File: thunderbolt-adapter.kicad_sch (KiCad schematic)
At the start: 16 parts

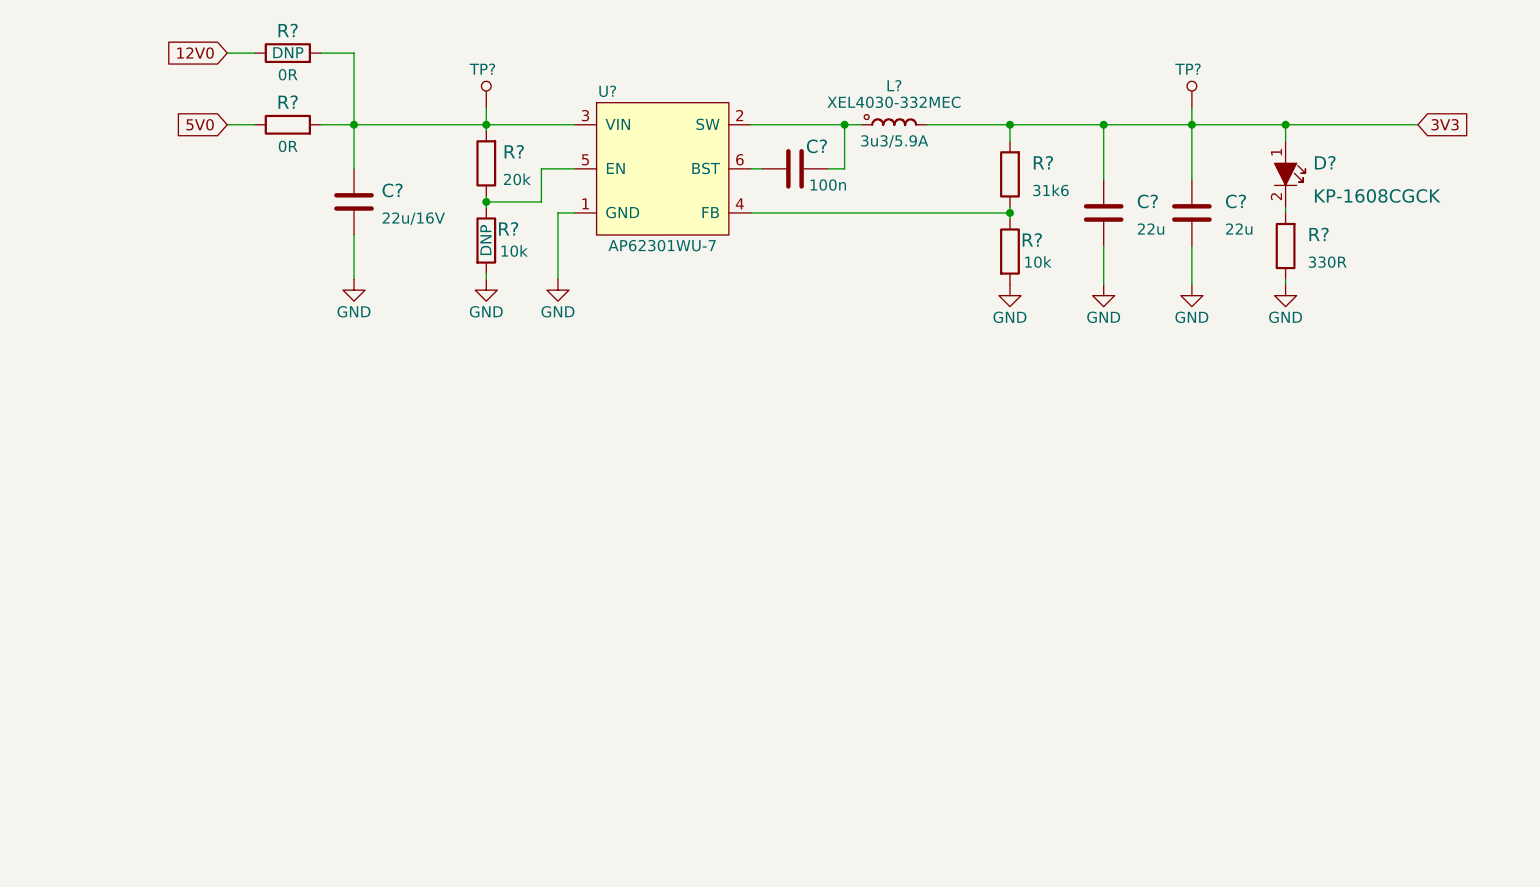
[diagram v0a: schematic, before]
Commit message: Add PCIe clock generator
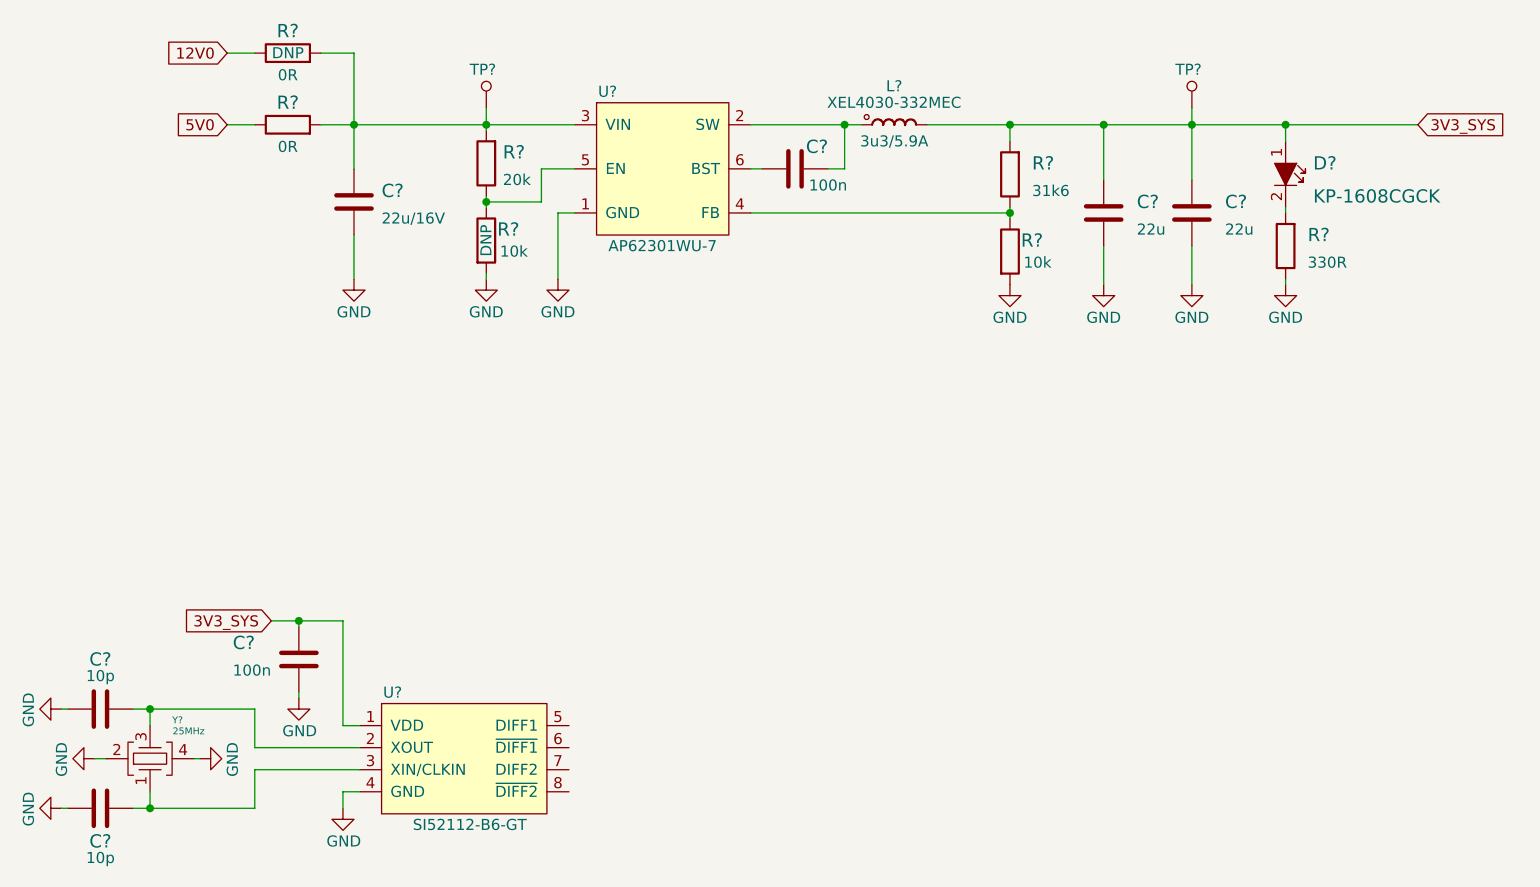
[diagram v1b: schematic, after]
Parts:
- added C? (x2): C_10p_0402, antmicro-footprints:0402-cap, symbol antmicroCapacitors0402:C_10p_0402
- added C?: C_100n_0402, antmicro-footprints:0402-cap, symbol antmicroCapacitors0402:C_100n_0402
- added U?: SI52112-B6-GT, antmicro-footprints:TSSOP-8_W4.4mm, symbol antmicroClockTimingClockGeneratorsPLLsFrequencySynthesizers:SI52112-B6-GT
- added Y?: 25MHz, antmicro-footprints:KX-7, symbol antmicroCrystals:ABM8G-25.000MHZ-B4Y-T
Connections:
- net GND: now also C?.1, C?.1, C?.2, U?.4 (GND), Y?.2, Y?.4
- net 3V3 renamed 3V3_SYS
- net 3V3_SYS: now also C?.1, U?.1 (VDD)
- new net: C?.2, U?.2 (XOUT), Y?.3
- new net: C?.2, U?.3 (XIN/CLKIN), Y?.1

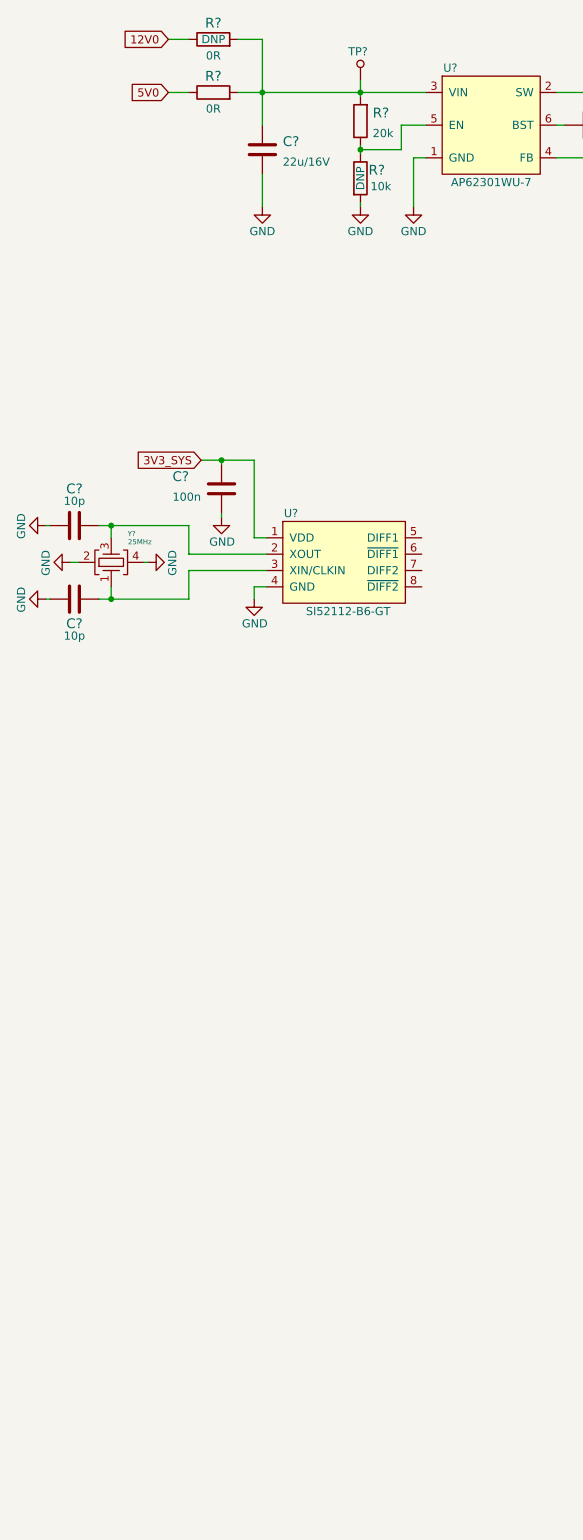
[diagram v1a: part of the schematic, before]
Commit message: Add USB-C connector
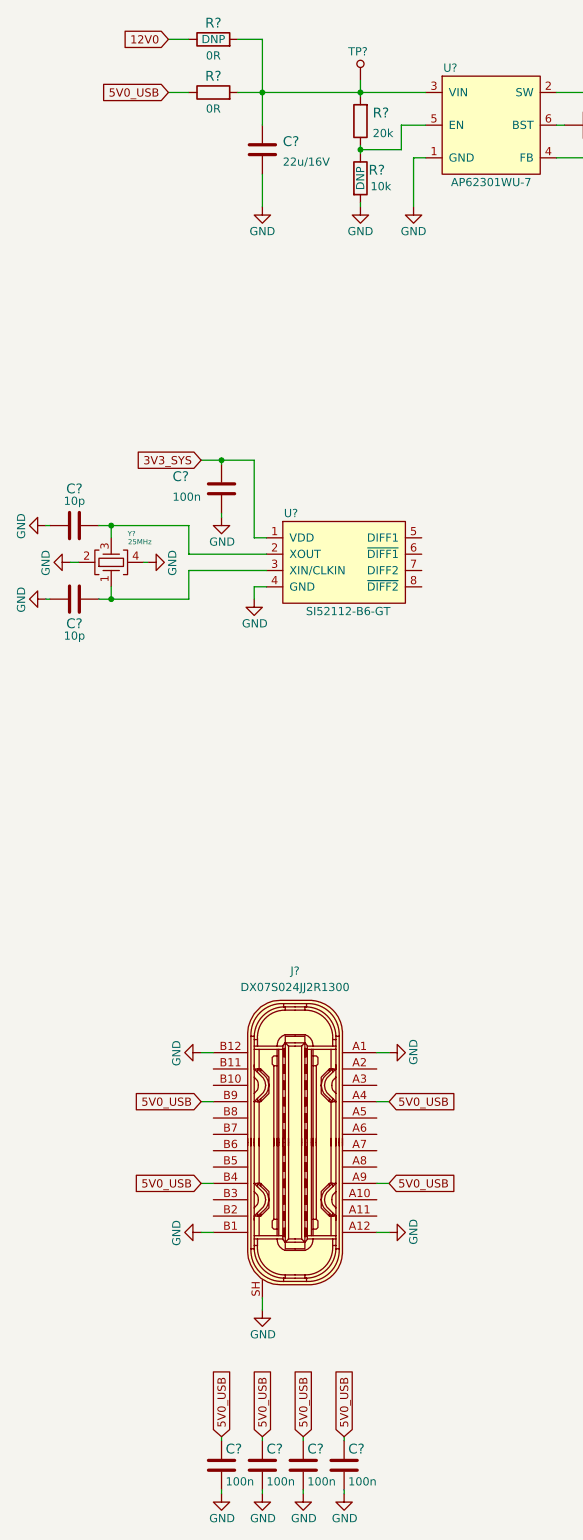
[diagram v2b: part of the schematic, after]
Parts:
- added C? (x4): C_100n_0402, antmicro-footprints:0402-cap, symbol antmicroCapacitors0402:C_100n_0402
- added J?: DX07S024JJ2R1300, antmicro-footprints:DX07S024JJ2R1300, symbol antmicroUSBDVIHDMIConnectors:DX07S024JJ2R1300
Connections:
- net GND: now also C?.2, C?.2, C?.2, C?.2, J?.A1, J?.A12, J?.B1, J?.B12, J?.SH
- net 5V0 renamed 5V0_USB
- net 5V0_USB: now also C?.1, C?.1, C?.1, C?.1, J?.A4, J?.A9, J?.B4, J?.B9

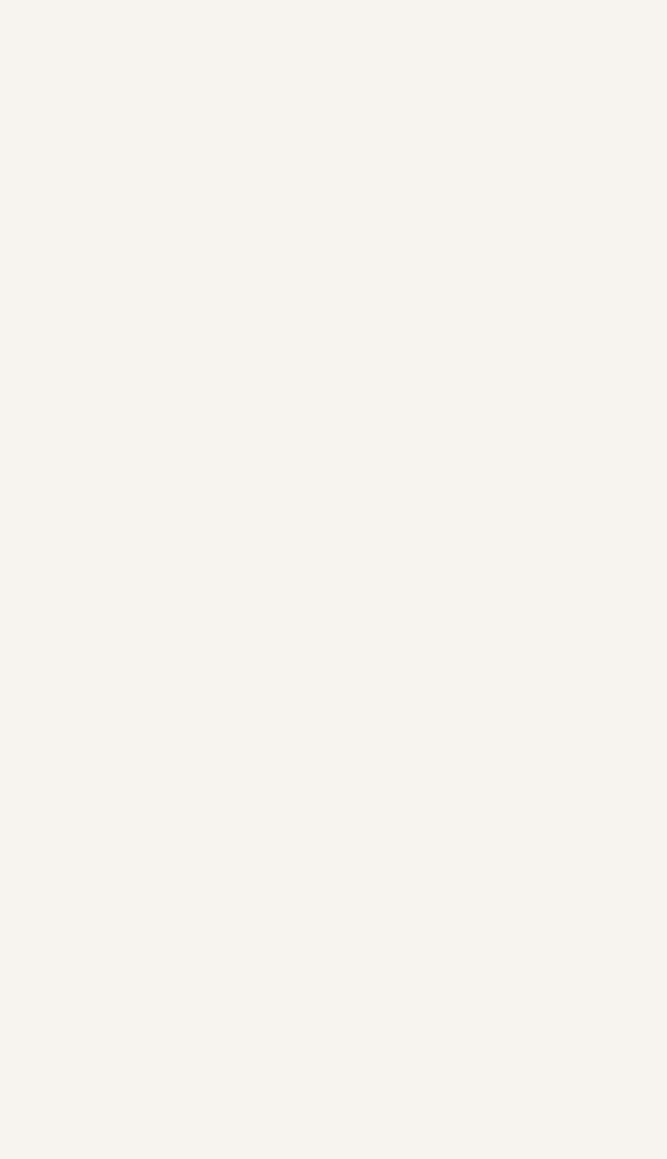
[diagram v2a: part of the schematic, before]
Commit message: Add PCIe edge connector
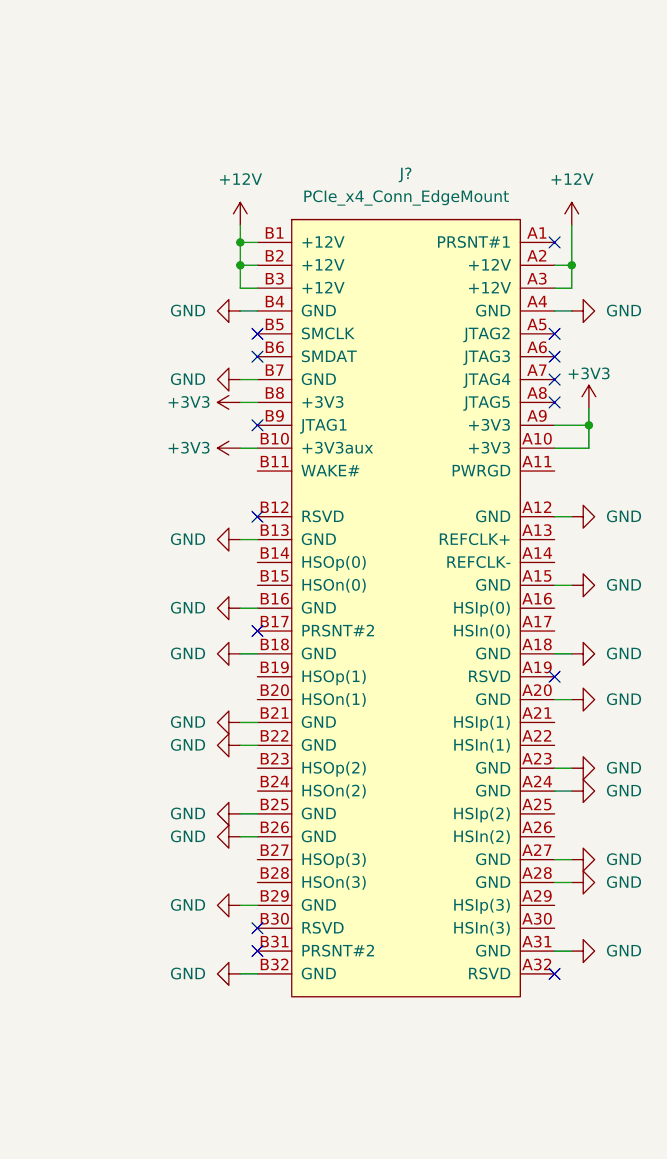
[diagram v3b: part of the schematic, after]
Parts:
- added J?: PCIe_x4_Conn_EdgeMount, antmicro-footprints:PCIE-064-02-X-D-EMSX, symbol antmicroPciConnectors:PCIe_x4_Conn_EdgeMount
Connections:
- net GND: now also J?.A12 (GND), J?.A15 (GND), J?.A18 (GND), J?.A20 (GND), J?.A23 (GND), J?.A24 (GND), J?.A27 (GND), J?.A28 (GND), J?.A31 (GND), J?.A4 (GND), J?.B13 (GND), J?.B16 (GND), J?.B18 (GND), J?.B21 (GND), J?.B22 (GND), J?.B25 (GND), J?.B26 (GND), J?.B29 (GND), J?.B32 (GND), J?.B4 (GND), J?.B7 (GND)
- new net +12V: J?.A2 (+12V), J?.A3 (+12V), J?.B1 (+12V), J?.B2 (+12V), J?.B3 (+12V)
- new net +3V3: J?.A10 (+3V3), J?.A9 (+3V3), J?.B10 (+3V3aux), J?.B8 (+3V3)
- no-connect marks 0 -> 14

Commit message: Add JHL6340SLLSQ, connect GND pins
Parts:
- added U? (x2): JHL6340SLLSQ, symbol antmicroInterfaceControllers:JHL6340SLLSQ
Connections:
- net +3V3 is gone; now on net 3V3_SYS: J?.A10 (+3V3), J?.A9 (+3V3), J?.B10 (+3V3aux), J?.B8 (+3V3)
- net 12V0 is gone; now on net 12V0_PCIE: R?.1
- net GND: now also U?.A1 (SVR_VSS), U?.A10 (VSS_ANA), U?.A12 (VSS_ANA), U?.A14 (VSS_ANA), U?.A16 (VSS_ANA), U?.A18 (VSS_ANA), U?.A20 (VSS_ANA), U?.A22 (VSS_ANA), U?.A6 (VSS_ANA), U?.A8 (VSS_ANA), U?.AA22 (VSS_ANA), U?.AA23 (VSS_ANA), U?.AB1 (VSS), U?.AB10 (VSS_ANA), U?.AB12 (VSS_ANA), U?.AB14 (VSS_ANA), U?.AB16 (VSS_ANA), U?.AB18 (VSS_ANA), U?.AB2 (MONDC_DPSRC), U?.AB20 (VSS_ANA), U?.AB22 (VSS_ANA), U?.AB6 (VSS_ANA), U?.AB8 (VSS_ANA), U?.AC1 (TEST_EDM), U?.AC10 (VSS_ANA), U?.AC12 (VSS_ANA), U?.AC14 (VSS_ANA), U?.AC16 (VSS_ANA), U?.AC18 (VSS_ANA), U?.AC2 (VSS), U?.AC20 (VSS_ANA), U?.AC22 (VSS_ANA), U?.AC6 (VSS_ANA), U?.AC8 (VSS_ANA), U?.B1 (SVR_VSS), U?.B10 (VSS_ANA), U?.B12 (VSS_ANA), U?.B14 (VSS_ANA), U?.B16 (VSS_ANA), U?.B18 (VSS_ANA), U?.B2 (SVR_VSS), U?.B20 (VSS_ANA), U?.B22 (VSS_ANA), U?.B6 (VSS_ANA), U?.B8 (VSS_ANA), U?.C22 (MONDC_CIO_1), U?.C23 (MONDC_CIO_0), U?.D11 (VSS_ANA), U?.D12 (VSS_ANA), U?.D13 (VSS_ANA), U?.D15 (VSS_ANA), U?.D16 (VSS_ANA), U?.D18 (VSS_ANA), U?.D5 (VSS), U?.D6 (MONDC_SVR), U?.D8 (VSS_ANA), U?.D9 (VSS_ANA), U?.E11 (VSS_ANA), U?.E15 (VSS_ANA), U?.E16 (VSS_ANA), U?.E22 (VSS_ANA), U?.E23 (VSS_ANA), U?.E4 (VSS), U?.E5 (VSS), U?.E6 (VSS), U?.E8 (VSS_ANA), U?.E9 (VSS_ANA), U?.F16 (VSS_ANA), U?.F20 (VSS_ANA), U?.F5 (VSS), U?.F6 (VSS), U?.F9 (VSS_ANA), U?.G22 (VSS_ANA), U?.G23 (VSS_ANA), U?.H1 (VSS_ANA), U?.H12 (VSS_ANA), U?.H13 (VSS_ANA), U?.H15 (VSS_ANA), U?.H16 (VSS_ANA), U?.H2 (VSS_ANA), U?.H20 (VSS_ANA), U?.H5 (VSS), U?.H8 (VSS), U?.J12 (VSS), U?.J13 (VSS), U?.J15 (VSS), U?.J18 (VSS_ANA), U?.J19 (VSS_ANA), U?.J20 (VSS_ANA), U?.J22 (VSS_ANA), U?.J23 (VSS_ANA), U?.J5 (VSS_ANA), U?.J8 (VSS), U?.K1 (VSS_ANA), U?.K2 (VSS_ANA), U?.L13 (VSS), U?.L15 (FUSE_VQPS_64), U?.L20 (VSS_ANA), U?.L22 (VSS_ANA), U?.L23 (VSS_ANA), U?.L5 (VSS_ANA), U?.M1 (VSS_ANA), U?.M11 (VSS), U?.M12 (VSS), U?.M19 (VSS_ANA), U?.M2 (VSS_ANA), U?.M20 (VSS_ANA), U?.M5 (VSS_ANA), U?.N11 (VSS), U?.N12 (VSS), U?.N13 (VSS), U?.N15 (FUSE_VQPS_128), U?.N20 (VSS_ANA), U?.N22 (VSS_ANA), U?.N23 (VSS_ANA), U?.N5 (VSS_ANA), U?.N8 (VSS), U?.N9 (VSS), U?.P1 (VSS_ANA), U?.P2 (VSS_ANA), U?.R18 (VSS_ANA), U?.R19 (VSS_ANA), U?.R20 (VSS_ANA), U?.R22 (VSS_ANA), U?.R23 (VSS_ANA), U?.R5 (VSS_ANA), U?.T1 (VSS_ANA), U?.T13 (VSS), U?.T15 (VSS), U?.T16 (VSS), U?.T18 (VSS), U?.T2 (VSS_ANA), U?.T20 (VSS_ANA), U?.T5 (VSS_ANA), U?.T6 (VSS), U?.T8 (VSS), U?.T9 (VSS), U?.U22 (VSS_ANA), U?.U23 (VSS_ANA), U?.V15 (VSS_ANA), U?.V16 (VSS_ANA), U?.V20 (VSS_ANA), U?.V5 (VSS_ANA), U?.V6 (VSS_ANA), U?.V8 (VSS_ANA), U?.V9 (VSS_ANA), U?.W13 (MONDC_DPSNK_0), U?.W18 (MONDC_DPSNK_1), U?.W20 (VSS_ANA), U?.W22 (VSS_ANA), U?.W23 (VSS_ANA), U?.W5 (VSS_ANA), U?.W6 (VSS_ANA), U?.W8 (VSS_ANA), U?.W9 (VSS_ANA), U?.Y13 (VSS_ANA), U?.Y20 (VSS_ANA), U?.Y9 (VSS_ANA)
- net +12V renamed 12V0_PCIE
